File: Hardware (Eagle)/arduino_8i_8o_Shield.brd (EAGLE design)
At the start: 68.6 x 53.3 mm, 15 parts, among them IC1 ULN2803

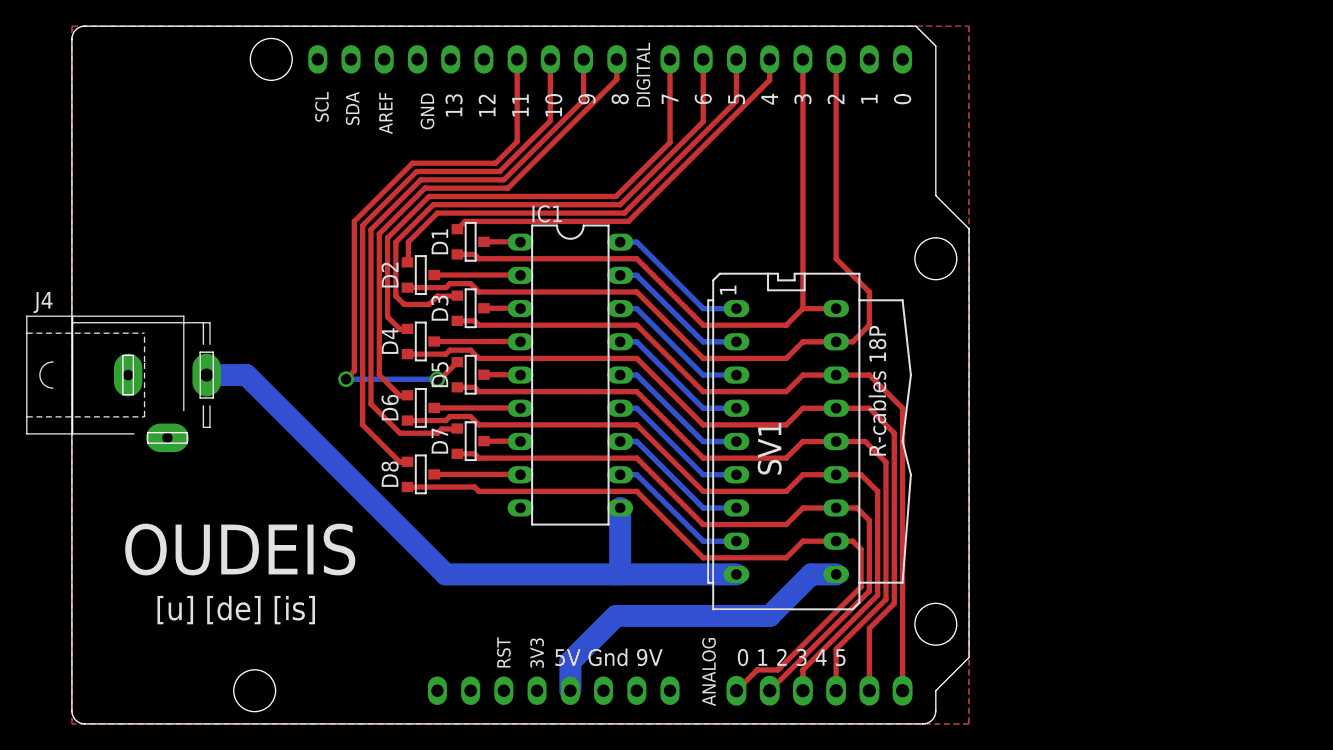
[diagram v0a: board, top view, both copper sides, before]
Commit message: Added 8 x 18k pull-down resistors on switches inputs
The absence of these resistors induced a cross talk between LED output
and switches reading inputs
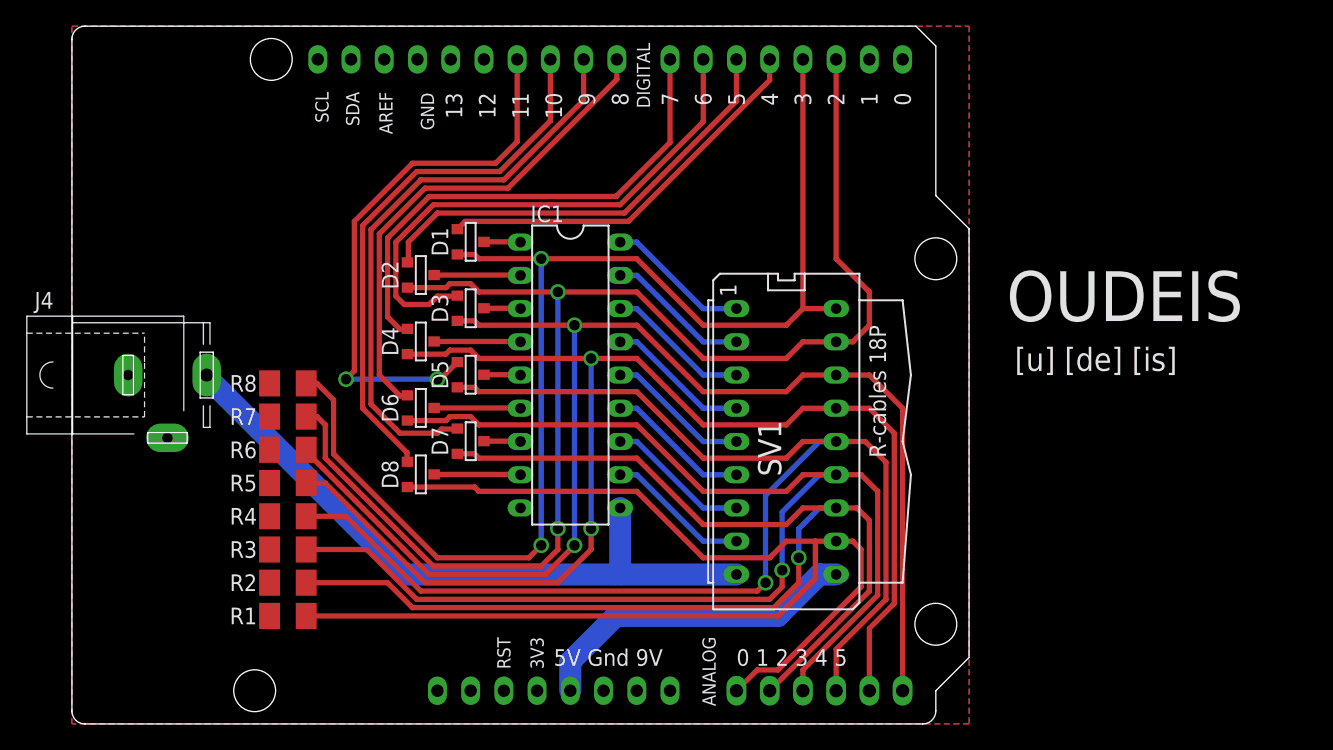
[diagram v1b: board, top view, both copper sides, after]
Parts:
- added R1, R2, R3, R4, R5, R6, R7, R8: 18k, rcl:M1206
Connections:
- net GND: now also R1.2, R2.2, R3.2, R4.2, R5.2, R6.2, R7.2, R8.2
- net SW0: now also R1.1
- net SW1: now also R2.1
- net SW2: now also R3.1
- net SW3: now also R4.1
- net SW4: now also R5.1
- net SW5: now also R6.1
- net SW6: now also R7.1
- net SW7: now also R8.1
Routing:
- net SW3: track 55.2 -> 106.7 mm, vias 0 -> 1
- net SW2: track 57.1 -> 106.5 mm, vias 0 -> 1
- net SW7: track 50.8 -> 99.0 mm, vias 0 -> 2
- net SW1: track 50.8 -> 97.7 mm, vias 0 -> 1
- net SW6: track 60.2 -> 105.9 mm, vias 0 -> 2
- net SW0: track 53.4 -> 96.3 mm
- net SW5: track 59.4 -> 101.7 mm, vias 0 -> 2
- net SW4: track 61.5 -> 102.1 mm, vias 0 -> 2
